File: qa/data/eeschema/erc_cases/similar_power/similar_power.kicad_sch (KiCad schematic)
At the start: 0 parts

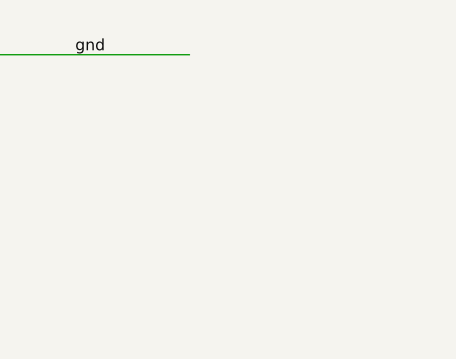
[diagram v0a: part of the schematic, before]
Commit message: qa: extend four ERC fixtures to reach what the S2-4b-7/8 sweep found unpinned
similar_labels gains a subsheet with a local daTa (case variants on two sheets are fine),
similar_power an ordinary part valued gnd (only power pins compare), symbol_pins a twin
whose duplicate pin numbers are jumpers, footprints a unit with no footprint and a
Resistor_SMD:R_* filter (a ':' filter matches the whole id). kicad-cli regenerated
every report; all match.

Co-Authored-By: Claude Opus 5.5 (1M context) <noreply@anthropic.com>
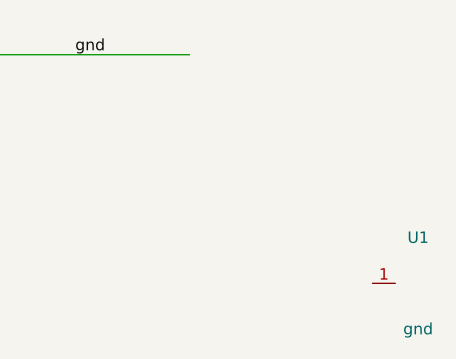
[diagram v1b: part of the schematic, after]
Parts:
- added U1: gnd, symbol erc:PART
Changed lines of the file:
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@@
 	(wire (pts (xy 101.6 76.2) (xy 127 76.2)) (stroke (width 0) (type default)))
 	(label "gnd" (at 114.3 76.2 0) (effects (font (size 1.27 1.27)) (justify left bottom)))
+	(symbol (lib_id "erc:PART") (at 152.4 101.6 0) (unit 1) (body_style 1) (exclude_from_sim no) (in_bom yes) (on_board yes) (dnp no)
+		(property "Reference" "U1" (at 152.4 96.52 0) (effects (font (size 1.27 1.27))))
+		(property "Value" "gnd" (at 152.4 106.68 0) (effects (font (size 1.27 1.27))))
+		(property "Footprint" "" (at 152.4 101.6 0) (hide yes) (effects (font (size 1.27 1.27))))
+		(property "Datasheet" "" (at 152.4 101.6 0) (hide yes) (effects (font (size 1.27 1.27))))
+		(pin "1")
+		(instances (project "similar_power" (path "/41111111-2222-3333-4444-555555555555" (reference "U1") (unit 1))))
+	)
 	(sheet_instances (path "/" (page "1")))
 )
